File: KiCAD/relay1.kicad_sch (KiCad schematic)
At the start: 15 parts, among them K1 SANYOU_SRD_Form_C, K2 SANYOU_SRD_Form_C, Q2 UMH3N, Q3 MMBT3906, Q4 MMBT3906

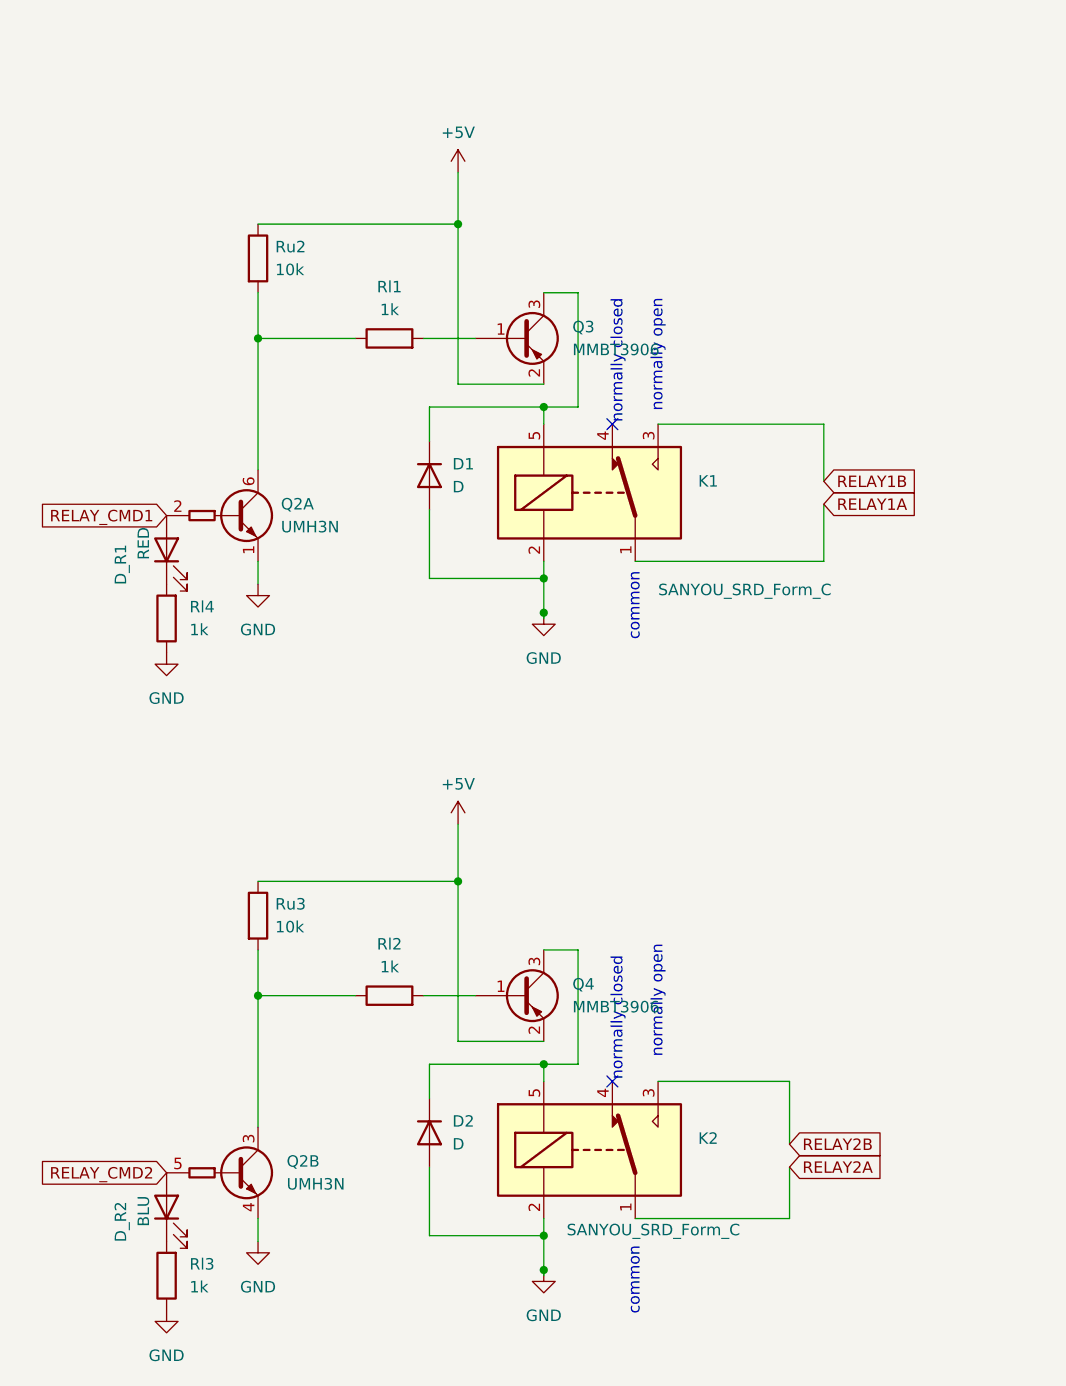
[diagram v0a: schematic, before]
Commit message: Updated KiCAD design
Fixes with help from Gemini.

- 2 sonars per side
- Divide-down echo signal to be 3V input-safe
- Fix pin assignments to non-straping pins for relay control, to avoid opening the garage
   door on power on(!)
- 1mm traces for relay nets, to be safer in case someone wires more power through these
   connections.
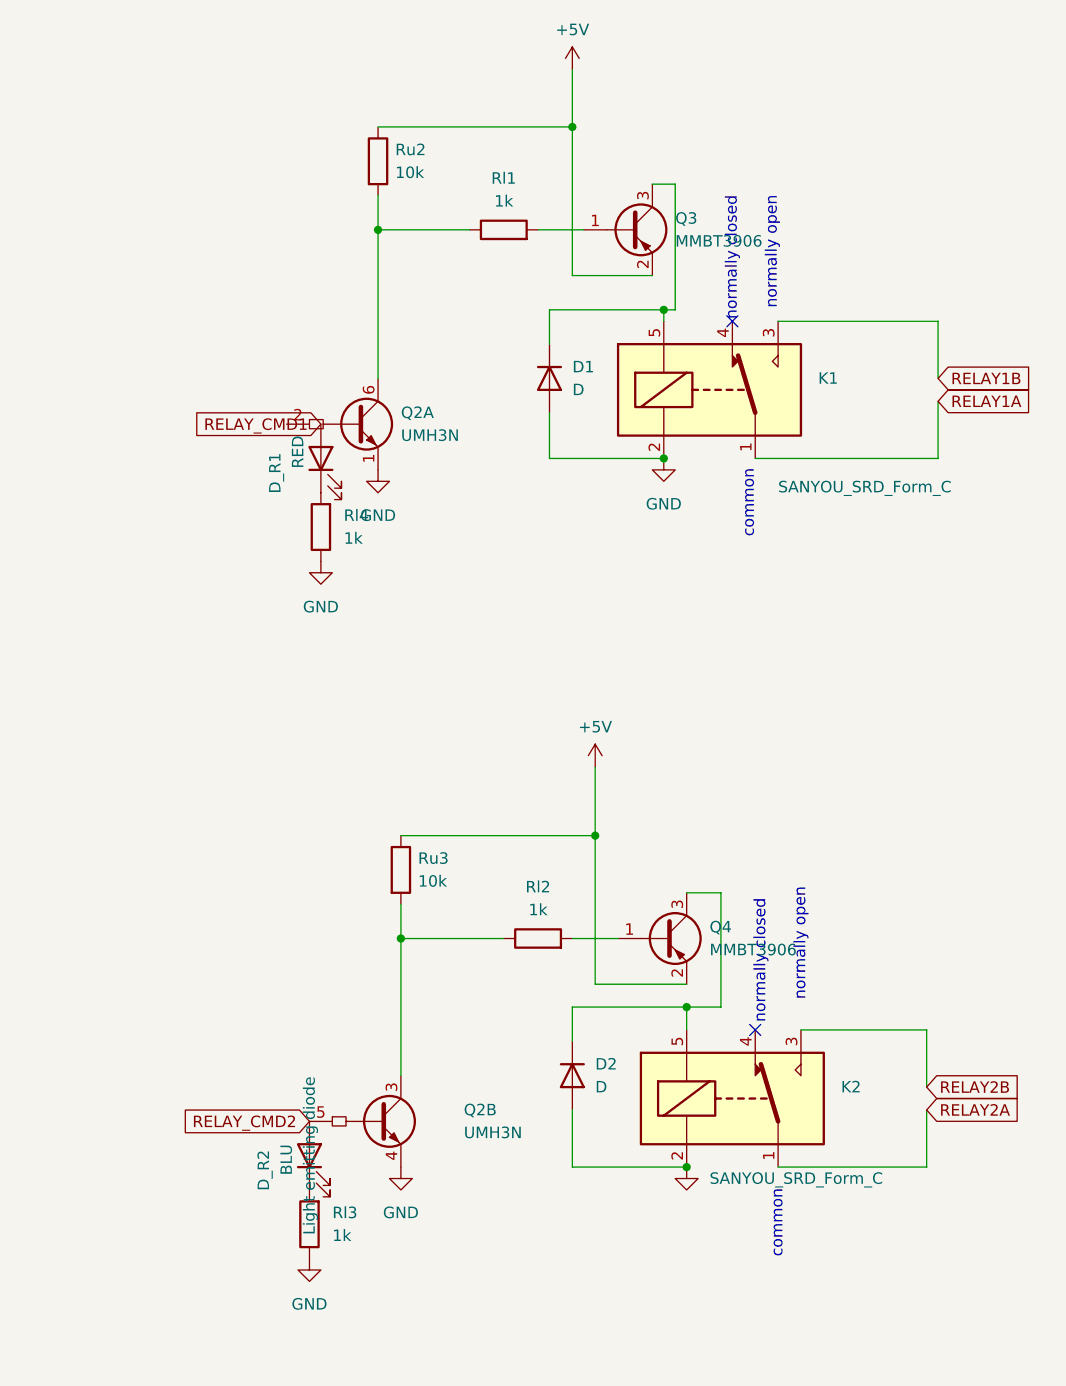
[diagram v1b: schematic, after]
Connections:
- net RELAY_CMD1: no longer Q2.2 (B1)
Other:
- moved on the sheet: D1, D2, D_R1, D_R2, K1, K2, Q2A, Q2B, Rl1, Rl2, Rl3, Rl4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

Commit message: KiCAD model: v2.1 fixes missing trace from Q2 pin2 to RELAY_CMD1
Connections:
- net RELAY_CMD1: now also Q2.2 (B1)
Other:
- moved on the sheet: D_R1, Rl4
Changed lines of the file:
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@@
 	(global_label "RELAY_CMD1"
 		(shape input)
-		(at 49.53 71.12 180)
+		(at 45.72 71.12 180)
 		(fields_autoplaced yes)
 		(effects
@@
 		)
 		(property "Intersheetrefs" "${INTERSHEET_REFS}"
-			(at 34.752 71.12 0)
+			(at 30.942 71.12 0)
 			(effects
 				(font
@@
 	(symbol
 		(lib_id "Device:LED")
-		(at 49.53 74.93 90)
+		(at 45.72 74.93 90)
 		(unit 1)
 		(exclude_from_sim no)
@@
 		(dnp no)
 		(property "Reference" "D_R1"
-			(at 44.45 74.295 0)
+			(at 40.64 74.295 0)
 			(effects
 				(font
@@
 		)
 		(property "Value" "RED"
-			(at 46.99 72.39 0)
+			(at 43.18 72.39 0)
 			(effects
 				(font
@@
 		)
 		(property "Footprint" "LED_SMD:LED_0603_1608Metric"
-			(at 49.53 74.93 0)
+			(at 45.72 74.93 0)
 			(effects
 				(font
@@
 		)
 		(property "Datasheet" "~"
-			(at 49.53 74.93 0)
+			(at 45.72 74.93 0)
 			(effects
 				(font
@@
 		)
 		(property "Description" "Light emitting diode"
-			(at 49.53 74.93 0)
+			(at 45.72 74.93 0)
 			(effects
 				(font
@@
 		)
 		(property "Sim.Pins" "1=K 2=A"
-			(at 49.53 74.93 0)
+			(at 45.72 74.93 0)
 			(effects
 				(font
@@
 	(symbol
 		(lib_id "power:GND")
-		(at 49.53 86.36 0)
+		(at 45.72 86.36 0)
 		(unit 1)
 		(exclude_from_sim no)
@@
 		(fields_autoplaced yes)
 		(property "Reference" "#PWR035"
-			(at 49.53 92.71 0)
+			(at 45.72 92.71 0)
 			(effects
 				(font
@@
 		)
 		(property "Value" "GND"
-			(at 49.53 91.44 0)
+			(at 45.72 91.44 0)
 			(effects
 				(font
@@
 		)
 		(property "Footprint" ""
-			(at 49.53 86.36 0)
+			(at 45.72 86.36 0)
 			(effects
 				(font
@@
 		)
 		(property "Datasheet" ""
-			(at 49.53 86.36 0)
+			(at 45.72 86.36 0)
 			(effects
 				(font
@@
 		)
 		(property "Description" "Power symbol creates a global label with name \"GND\" , ground"
-			(at 49.53 86.36 0)
+			(at 45.72 86.36 0)
 			(effects
 				(font
@@
 	(symbol
 		(lib_id "Device:R")
-		(at 49.53 82.55 180)
+		(at 45.72 82.55 180)
 		(unit 1)
 		(exclude_from_sim no)
@@
 		(fields_autoplaced yes)
 		(property "Reference" "Rl4"
-			(at 52.07 81.28 0)
+			(at 48.26 81.28 0)
 			(effects
 				(font
@@
 		)
 		(property "Value" "1k"
-			(at 52.07 83.82 0)
+			(at 48.26 83.82 0)
 			(effects
 				(font
@@
 		)
 		(property "Footprint" "Resistor_SMD:R_0603_1608Metric"
-			(at 51.308 82.55 90)
+			(at 47.498 82.55 90)
 			(effects
 				(font
@@
 		)
 		(property "Datasheet" "~"
-			(at 49.53 82.55 0)
+			(at 45.72 82.55 0)
 			(effects
 				(font
@@
 		)
 		(property "Description" ""
-			(at 49.53 82.55 0)
-			(effects
-				(font
+			(at 45.72 82.55 0)
+			(effects
+				(font
